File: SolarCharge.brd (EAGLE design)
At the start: 46 x 92 mm, 22 parts, among them U1 TINY4/5/9/10-TSHR/TS8R

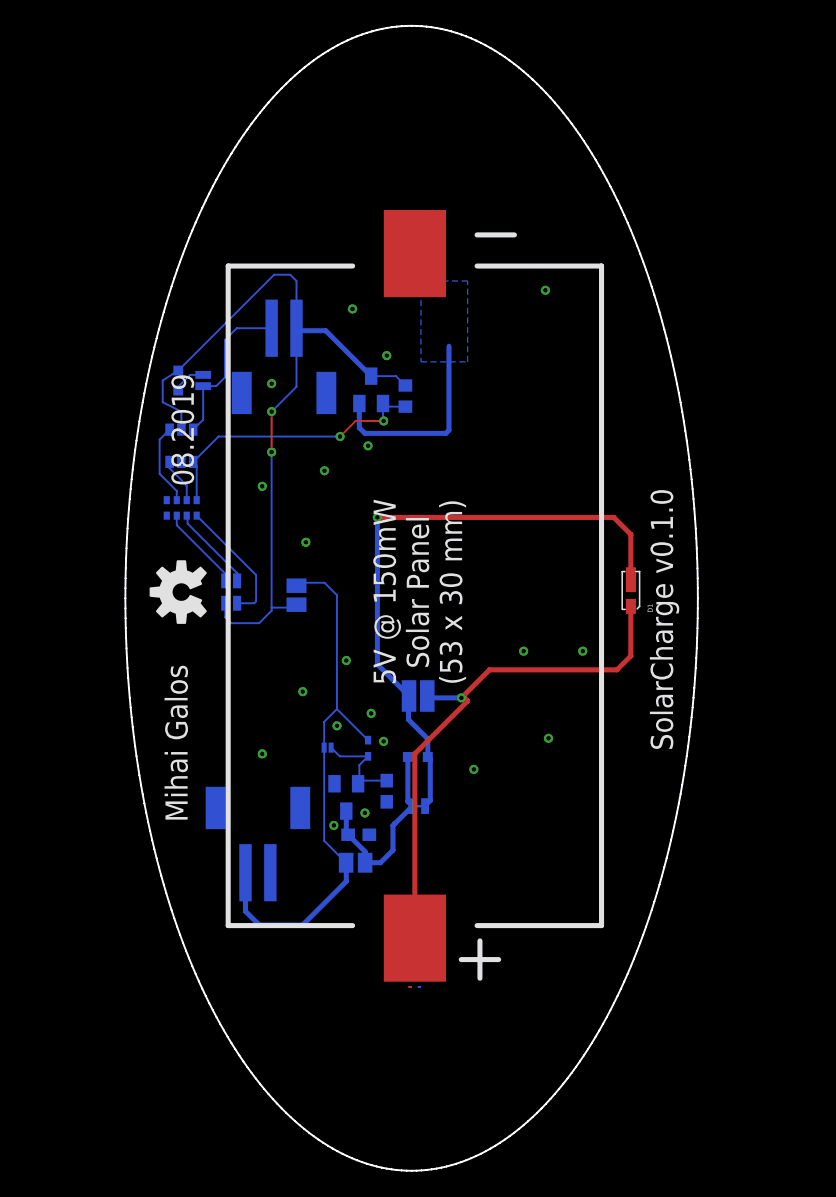
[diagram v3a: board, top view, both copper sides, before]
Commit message: Correct position of graphics, add pads for boost converter
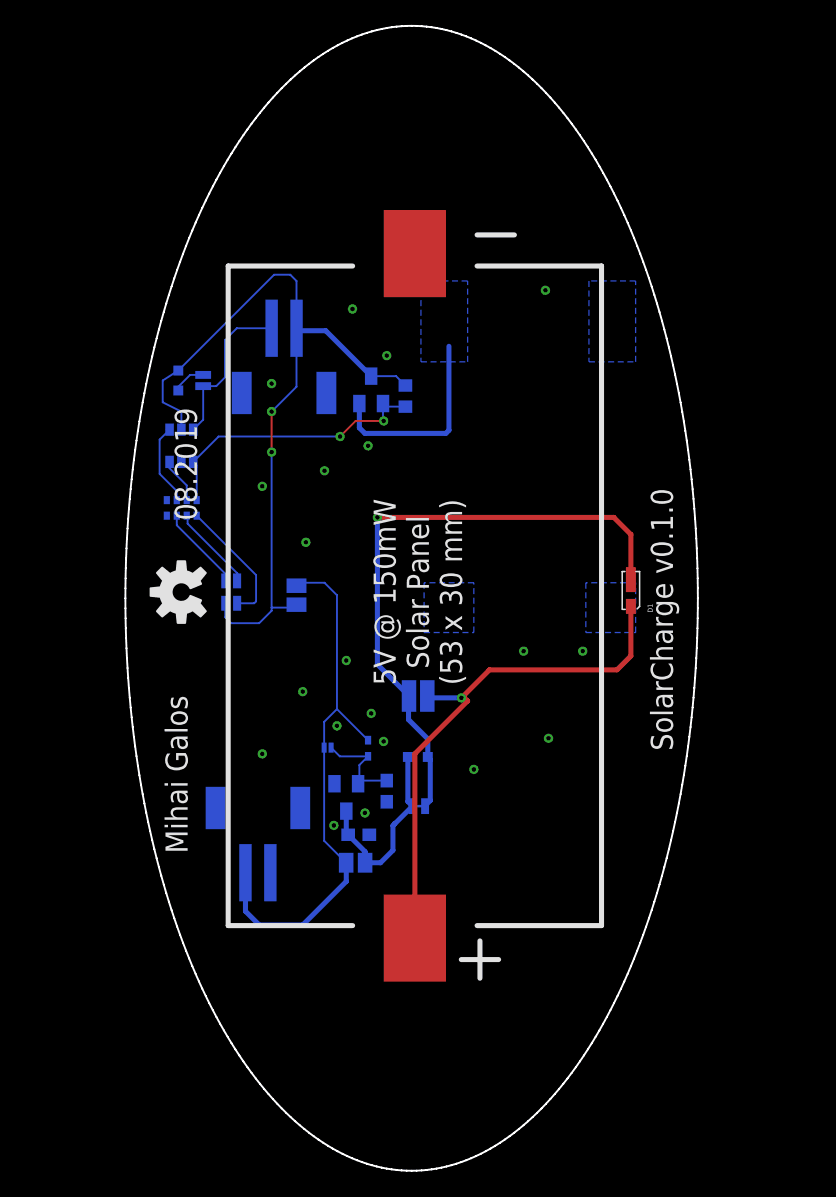
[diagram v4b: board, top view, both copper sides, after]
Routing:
- added copper zone on layer 16, net PAD_BOOST1
- added copper zone on layer 16, net PAD_BOOST2
- added copper zone on layer 16, net PAD_BOOST3
- removed copper zone on layer 1, net GND
- removed copper zone on layer 16, net GND
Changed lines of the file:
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@@
 <board>
 <plain>
-<text x="2.5" y="40" size="1.778" layer="21" rot="R90">08.2019</text>
+<text x="2.75" y="37.25" size="1.778" layer="21" rot="R90">08.2019</text>
 <text x="41" y="18.75" size="1.778" layer="21" rot="R90">SolarCharge v0.1.0</text>
 <text x="20.5" y="31.5" size="1.778" layer="21" rot="R90" align="center">5V @ 150mW
@@
 <dimension x1="20" y1="-15" x2="20" y2="77" x3="48.25" y3="31" textsize="1.778" layer="47"/>
 <dimension x1="-3" y1="31" x2="43" y2="31" x3="20" y3="77" textsize="1.778" layer="47"/>
-<text x="2" y="13" size="1.778" layer="21" rot="R90">Mihai Galos</text>
+<text x="2" y="10.5" size="1.778" layer="21" rot="R90">Mihai Galos</text>
 </plain>
 <attributes>
@@
 <wire x1="22.5" y1="56.46" x2="20.26" y2="58.7" width="0.4064" layer="1"/>
 <contactref element="CN1" pad="2"/>
-<polygon width="0.6096" layer="1">
-<vertex x="19.75" y="-0.25"/>
-<vertex x="20" y="-0.25" curve="90"/>
-</polygon>
-<polygon width="0.6096" layer="16">
-<vertex x="20.5" y="-0.25"/>
-<vertex x="20.75" y="-0.25" curve="90"/>
-</polygon>
 <via x="8.75" y="48.25" extent="1-16" drill="0.35"/>
 <via x="8" y="40" extent="1-16" drill="0.35"/>
@@
 <via x="13.75" y="12.75" extent="1-16" drill="0.35"/>
 <via x="16.25" y="13.75" extent="1-16" drill="0.35"/>
+<wire x1="22.5" y1="56.46" x2="30.75" y2="55.75" width="0" layer="19" extent="1-1"/>
+<wire x1="15.25" y1="54.25" x2="20.26" y2="58.7" width="0" layer="19" extent="1-1"/>
+<wire x1="18" y1="50.5" x2="15.25" y2="54.25" width="0" layer="19" extent="1-1"/>
+<wire x1="16.5" y1="43.25" x2="18" y2="50.5" width="0" layer="19" extent="1-1"/>
+<wire x1="13" y1="41.25" x2="16.5" y2="43.25" width="0" layer="19" extent="1-1"/>
+<wire x1="8" y1="40" x2="13" y2="41.25" width="0" layer="19" extent="1-1"/>
+<wire x1="11.5" y1="35.5" x2="8" y2="40" width="0" layer="19" extent="1-1"/>
+<wire x1="1.5" y1="41.96" x2="8" y2="40" width="0" layer="19" extent="16-16"/>
+<wire x1="8.75" y1="48.25" x2="13" y2="41.25" width="0" layer="19" extent="1-1"/>
+<wire x1="14.75" y1="26" x2="11.5" y2="35.5" width="0" layer="19" extent="1-1"/>
+<wire x1="11.25" y1="23.5" x2="14.75" y2="26" width="0" layer="19" extent="1-1"/>
+<wire x1="14" y1="20.75" x2="11.25" y2="23.5" width="0" layer="19" extent="1-1"/>
+<wire x1="16.75" y1="21.75" x2="14" y2="20.75" width="0" layer="19" extent="1-1"/>
+<wire x1="17.75" y1="19.5" x2="16.75" y2="21.75" width="0" layer="19" extent="1-1"/>
+<wire x1="13.8" y1="16.1" x2="14" y2="20.75" width="0" layer="19" extent="16-16"/>
+<wire x1="13.75" y1="12.75" x2="13.8" y2="16.1" width="0" layer="19" extent="16-16"/>
+<wire x1="16.25" y1="13.75" x2="13.75" y2="12.75" width="0" layer="19" extent="1-1"/>
+<wire x1="16.6" y1="12" x2="16.25" y2="13.75" width="0" layer="19" extent="16-16"/>
+<wire x1="18" y1="14.65" x2="16.25" y2="13.75" width="0" layer="19" extent="16-16"/>
+<wire x1="8" y1="18.5" x2="11.25" y2="23.5" width="0" layer="19" extent="1-1"/>
+<wire x1="8.65" y1="8.95" x2="13.75" y2="12.75" width="0" layer="19" extent="16-16"/>
+<wire x1="25" y1="17.25" x2="18" y2="14.65" width="0" layer="19" extent="16-16"/>
+<wire x1="31" y1="19.75" x2="25" y2="17.25" width="0" layer="19" extent="1-1"/>
+<wire x1="29" y1="26.75" x2="31" y2="19.75" width="0" layer="19" extent="1-1"/>
+<wire x1="33.75" y1="26.75" x2="29" y2="26.75" width="0" layer="19" extent="1-1"/>
 </signal>
 <signal name="N$3">
@@
 <wire x1="12.9706" y1="11.5174" x2="14.75" y2="9.738" width="0.1524" layer="16"/>
 </signal>
+<signal name="PAD_BOOST1">
+<polygon width="0.4064" layer="16">
+<vertex x="34.25" y="50"/>
+<vertex x="38" y="50"/>
+<vertex x="38" y="56.5"/>
+<vertex x="34.25" y="56.5"/>
+</polygon>
+</signal>
+<signal name="PAD_BOOST2">
+<polygon width="0.4064" layer="16">
+<vertex x="21" y="28.25"/>
+<vertex x="25" y="28.25"/>
+<vertex x="25" y="32.25"/>
+<vertex x="21" y="32.25"/>
+</polygon>
+</signal>
+<signal name="PAD_BOOST3">
+<polygon width="0.4064" layer="16">
+<vertex x="34" y="28.25"/>
+<vertex x="38" y="28.25"/>
+<vertex x="38" y="32.25"/>
+<vertex x="34" y="32.25"/>
+</polygon>
+</signal>
 </signals>

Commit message: Readd gnd planes for ellipse
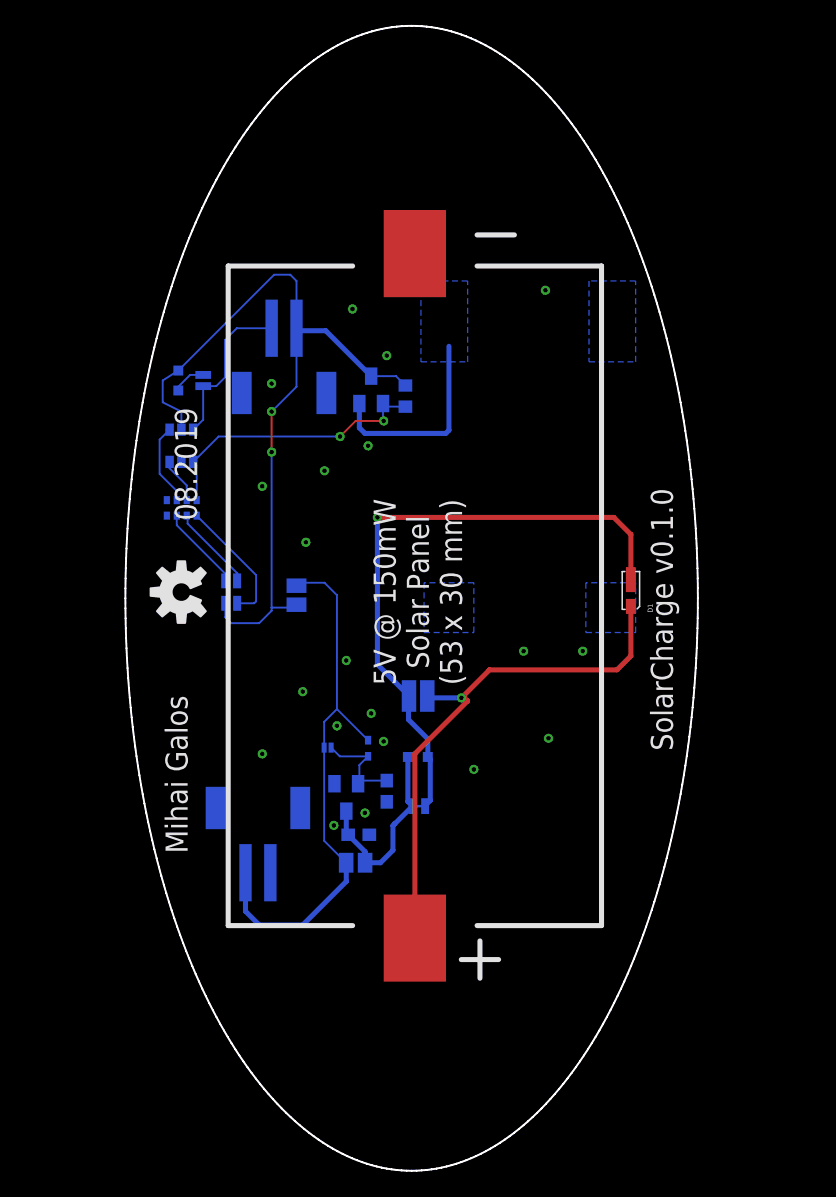
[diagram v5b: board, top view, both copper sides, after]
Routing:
- added copper zone on layer 1, net GND
- added copper zone on layer 16, net GND
